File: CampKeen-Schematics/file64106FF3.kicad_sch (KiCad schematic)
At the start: 9 parts, among them Q8 2N7000, Q9 IRF9Z34NPBF

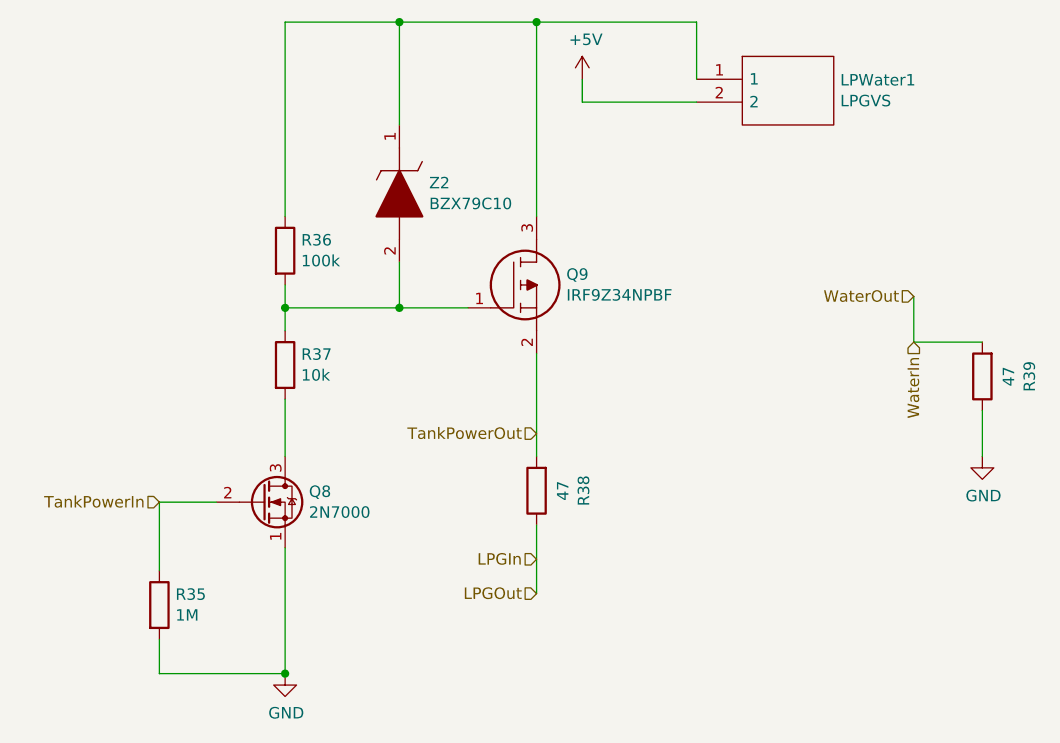
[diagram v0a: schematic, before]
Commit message: alright massive changes. some part switches and some reassignments. mostly it's switching out stuff for SMD so that i have more space.
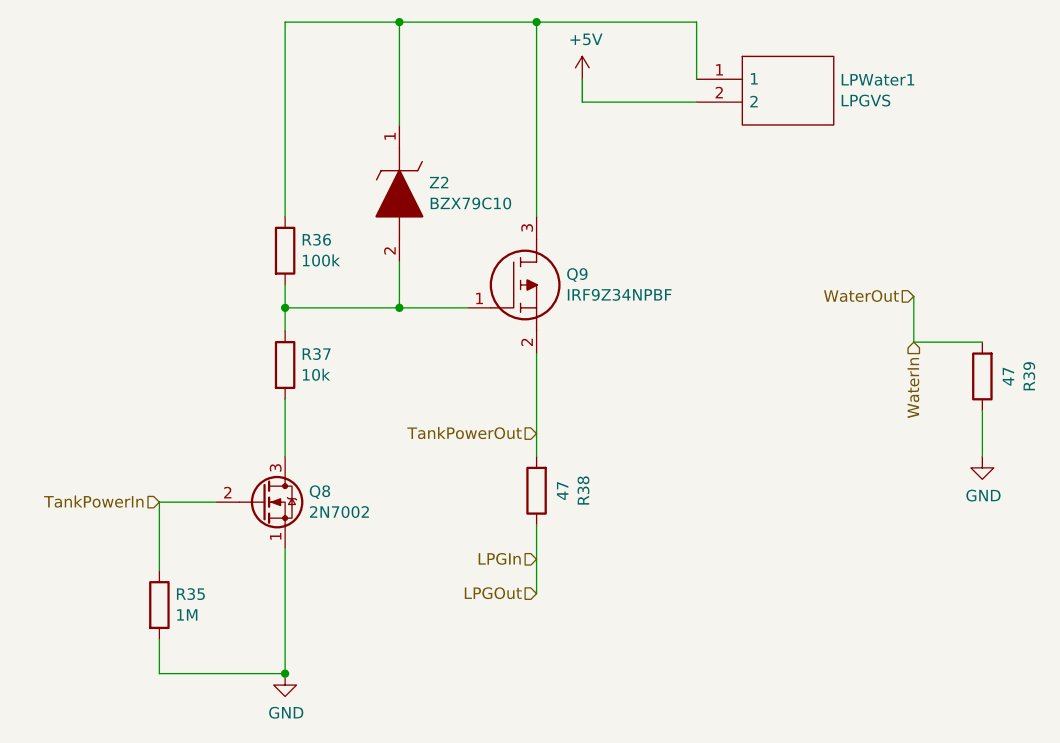
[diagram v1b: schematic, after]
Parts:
- Q8: value 2N7000 -> 2N7002; footprint Package_TO_SOT_THT:TO-92_Inline -> Package_TO_SOT_SMD:SOT-23
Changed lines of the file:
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@@
       (effects (font (size 1.27 1.27)) (justify left))
     )
-    (property "Value" "2N7000" (id 1) (at 71.2216 105.283 0)
+    (property "Value" "2N7002" (id 1) (at 71.2216 105.283 0)
       (effects (font (size 1.27 1.27)) (justify left))
     )
-    (property "Footprint" "Package_TO_SOT_THT:TO-92_Inline" (id 2) (at 71.12 106.045 0)
+    (property "Footprint" "Package_TO_SOT_SMD:SOT-23" (id 2) (at 71.12 106.045 0)
       (effects (font (size 1.27 1.27) italic) (justify left) hide)
     )
